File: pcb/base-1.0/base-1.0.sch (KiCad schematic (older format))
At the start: 80 parts, among them J101 USB_B_Micro, J102 UART, J103 74984104400, J104 Jack-DC, J105 USB_GPIO, J106 Raspberry_Pi_2_3, Q101 BC817, Q102 BC817, Q103 DMP2305U-7, SW101 SW_Push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

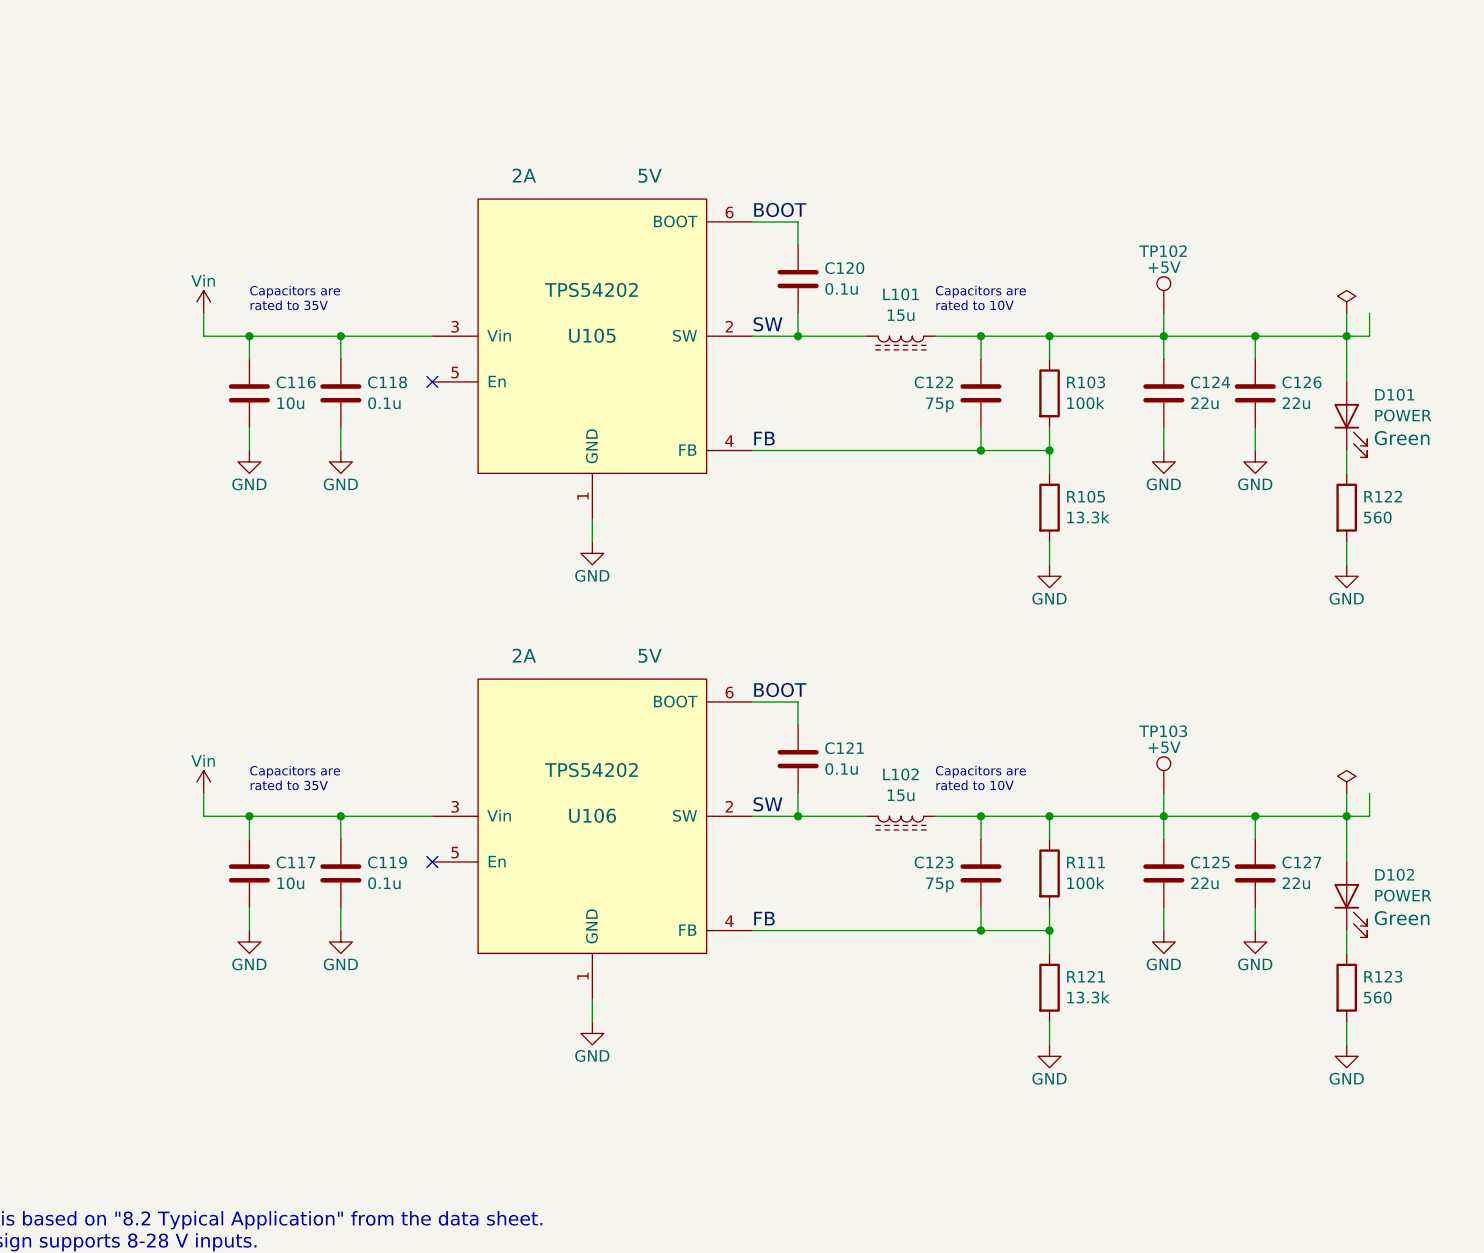
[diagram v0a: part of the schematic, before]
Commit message: o Adjusting text size from 60 to 50 mil for imported DC/DC schematic.
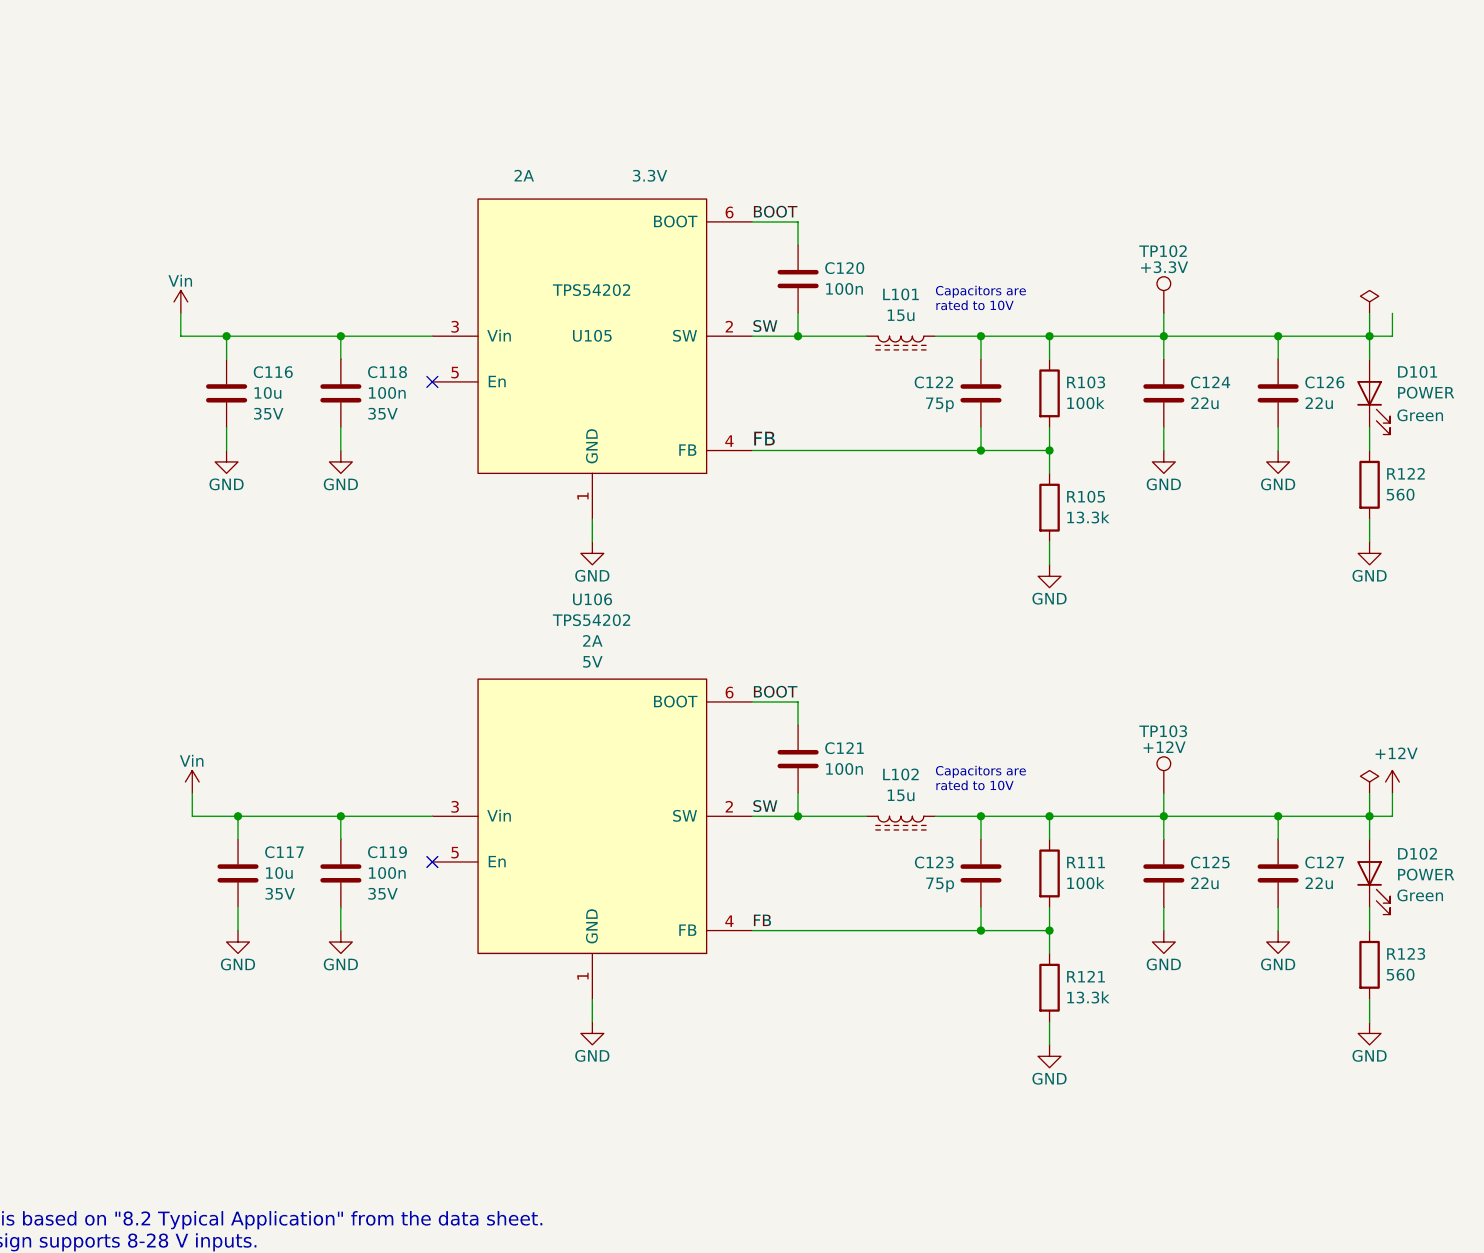
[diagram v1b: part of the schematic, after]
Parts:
- C118, C119, C120, C121: value 0.1u -> 100n
- TP102: value +5V -> +3.3V
- TP103: value +5V -> +12V
- U105: Vout 5V -> 3.3V
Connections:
- net +12V: now reaches C123.1, C125.1, C127.1, D102.2 (A), L102.1, R111.1, TP103.1
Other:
- note removed: "Capacitors are\nrated to 35V"
- moved on the sheet: C116, C117, C126, C127, D101, D102, R122, R123

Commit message: o More values.
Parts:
- C104: value C -> 1n; voltage (none) -> 2kV
- C113: value C -> ~
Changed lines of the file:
@@
 U 1 1 5DBE189D
 P 1900 10750
-F 0 "C104" H 2015 10796 50  0000 L CNN
-F 1 "C" H 2015 10705 50  0000 L CNN
+F 0 "C104" H 2015 10841 50  0000 L CNN
+F 1 "1n" H 2015 10750 50  0000 L CNN
 F 2 "IPC-7351-CAPC:CAPC_1005x015" H 1938 10600 50  0001 C CNN
 F 3 "~" H 1900 10750 50  0001 C CNN
+F 4 "2kV" H 2015 10659 50  0000 L CNN "voltage"
 	1    1900 10750
 	1    0    0    -1
@@
 U 1 1 5CEB2CA9
 P 700 2650
-F 0 "C113" H 815 2741 50  0000 L CNN
-F 1 "C" H 815 2650 50  0000 L CNN
+F 0 "C113" H 815 2696 50  0000 L CNN
+F 1 "~" H 815 2650 50  0000 L CNN
 F 2 "IPC-7351-CAPC:CAPC_1005x015" H 738 2500 50  0001 C CNN
 F 3 "~" H 700 2650 50  0001 C CNN
-F 4 "DNP" H 815 2559 50  0000 L CNN "populate"
+F 4 "DNP" H 815 2605 50  0000 L CNN "populate"
 	1    700  2650
 	1    0    0    -1

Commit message: o More values.
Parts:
- R106, R107: value R -> 120 Ω
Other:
- moved on the sheet: D104, R107
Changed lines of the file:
@@
 Text Label 5600 2700 0    50   ~ 0
 TXT
-$Comp
-L Device:LED D104
-U 1 1 5CC3EC2A
-P 7300 1950
-F 0 "D104" H 7293 1788 50  0000 C CNN
-F 1 "TX" H 7293 1697 50  0000 C CNN
-F 2 "IPC-7351-LEDSC:LEDSC_3216x060" H 7300 1950 50  0001 C CNN
-F 3 "~" H 7300 1950 50  0001 C CNN
-	1    7300 1950
-	0    -1   -1   0
-$EndComp
-$Comp
-L Device:R R107
-U 1 1 5CD8FDB9
-P 7300 2350
-F 0 "R107" V 7415 2350 50  0000 C CNN
-F 1 "R" V 7506 2350 50  0000 C CNN
-F 2 "IPC-7351-RESC:RESC_1005x015" V 7230 2350 50  0001 C CNN
-F 3 "~" H 7300 2350 50  0001 C CNN
-	1    7300 2350
-	1    0    0    -1
-$EndComp
-Wire Wire Line
-	7300 2200 7300 2100
 Wire Wire Line
 	7100 2200 7100 2100
-$Comp
-L Device:R R106
-U 1 1 5CD8FFCC
-P 7100 2350
-F 0 "R106" V 7307 2350 50  0000 C CNN
-F 1 "R" V 7216 2350 50  0000 C CNN
-F 2 "IPC-7351-RESC:RESC_1005x015" V 7030 2350 50  0001 C CNN
-F 3 "~" H 7100 2350 50  0001 C CNN
-	1    7100 2350
-	-1   0    0    1
-$EndComp
-$Comp
-L Device:LED D103
-U 1 1 5CC3BC53
-P 7100 1950
-F 0 "D103" H 7093 2166 50  0000 C CNN
-F 1 "RX" H 7093 2075 50  0000 C CNN
-F 2 "IPC-7351-LEDSC:LEDSC_3216x060" H 7100 1950 50  0001 C CNN
-F 3 "~" H 7100 1950 50  0001 C CNN
-	1    7100 1950
-	0    -1   -1   0
-$EndComp
 Wire Wire Line
 	4300 900  4900 900
@@
 Wire Wire Line
 	7100 1600 7100 1700
-Wire Wire Line
-	7300 1800 7300 1700
-Wire Wire Line
-	7300 1700 7100 1700
 Connection ~ 7100 1700
 Wire Wire Line
@@
 	7100 2500 7100 2600
 Wire Wire Line
-	7300 2500 7300 2700
-Wire Wire Line
 	5600 2600 7100 2600
-Wire Wire Line
-	5600 2700 7300 2700
 $Comp
 L Device:Q_NPN_BEC Q102
@@
 	1    0    0    -1
 $EndComp
+$Comp
+L Device:LED D103
+U 1 1 5CC3BC53
+P 7100 1950
+F 0 "D103" V 7139 1832 50  0000 R CNN
+F 1 "RX" V 7048 1832 50  0000 R CNN
+F 2 "IPC-7351-LEDSC:LEDSC_3216x060" H 7100 1950 50  0001 C CNN
+F 3 "~" H 7100 1950 50  0001 C CNN
+	1    7100 1950
+	0    -1   -1   0
+$EndComp
+Wire Wire Line
+	5600 2700 7500 2700
+Wire Wire Line
+	7500 2500 7500 2700
+Wire Wire Line
+	7500 1700 7100 1700
+Wire Wire Line
+	7500 1800 7500 1700
+Wire Wire Line
+	7500 2200 7500 2100
+$Comp
+L Device:LED D104
+U 1 1 5CC3EC2A
+P 7500 1950
+F 0 "D104" V 7539 1832 50  0000 R CNN
+F 1 "TX" V 7448 1832 50  0000 R CNN
+F 2 "IPC-7351-LEDSC:LEDSC_3216x060" H 7500 1950 50  0001 C CNN
+F 3 "~" H 7500 1950 50  0001 C CNN
+	1    7500 1950
+	0    -1   -1   0
+$EndComp
+$Comp
+L Device:R R106
+U 1 1 5CD8FFCC
+P 7100 2350
+F 0 "R106" H 7030 2304 50  0000 R CNN
+F 1 "120 Ω" H 7030 2395 50  0000 R CNN
+F 2 "IPC-7351-RESC:RESC_1005x015" V 7030 2350 50  0001 C CNN
+F 3 "~" H 7100 2350 50  0001 C CNN
+	1    7100 2350
+	-1   0    0    1
+$EndComp
+$Comp
+L Device:R R107
+U 1 1 5CD8FDB9
+P 7500 2350
+F 0 "R107" H 7570 2396 50  0000 L CNN
+F 1 "120 Ω" H 7570 2305 50  0000 L CNN
+F 2 "IPC-7351-RESC:RESC_1005x015" V 7430 2350 50  0001 C CNN
+F 3 "~" H 7500 2350 50  0001 C CNN
+	1    7500 2350
+	1    0    0    -1
+$EndComp

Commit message: o Selecting parts.
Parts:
- C101: value 100n -> 100nF; mpn (none) -> CL05B104KO5NNNC
- C102: value 10u -> 10uF; footprint IPC-7351-CAPC:CAPC_1005x015 -> IPC-7351-CAPC:CAPC_2012x040; mpn (none) -> CL21B106KOQNNNE
- C104: value 1n -> 1nF; Voltage (none) -> 2kV; mpn (none) -> C1812C102KGRACAUTO; voltage 2kV -> (none)
- C105: mpn (none) -> CL05B471JB5NNNC
- C106, C109: mpn (none) -> CL05A105MQ5NNNC
- C107, C110, C111, C112, C115: mpn (none) -> CL05B104KO5NNNC
- C114: value 1u -> 1uF; mpn (none) -> CL05A105MQ5NNNC
- C116, C117: value 10u -> 10uF; Voltage (none) -> 35V; req_voltage 35V -> (none)
- C118, C119: value 100n -> 100nF; Voltage (none) -> 35V; mpn GMK212BJ104KGHT -> CL21B104MBCNNNC; req_voltage 35V -> (none)
- C120: value 100n -> 100nF; footprint IPC-7351-CAPC:CAPC_2012x040 -> IPC-7351-CAPC:CAPC_1005x015; Voltage (none) -> 35V; req_voltage (none) -> 10V; voltage 10V -> (none)
- C121: value 100n -> 100nF; footprint IPC-7351-CAPC:CAPC_2012x040 -> IPC-7351-CAPC:CAPC_1005x015; Voltage (none) -> 35V; req_voltage (none) -> 25V; voltage 10V -> (none)
- C122: value 75p -> 56pF; Voltage (none) -> 10V; mpn GRM1555C1H750JA01D -> CL05C560JB5NNNC; voltage 10V -> (none)
- C123: value 75p -> 100pF; Voltage (none) -> 25V; mpn GRM1555C1H750JA01D -> CL05C101JB5NNNC; voltage 10V -> (none)
- C124, C126: value 22u -> 22uF; Voltage (none) -> 10V; voltage 10V -> (none)
- C125, C127: value 22u -> 22uF; Voltage (none) -> 25V; voltage 10V -> (none)
- D101: I (none) -> 5 mA; V (none) -> 3.3; ds_Vf 2.1 V -> (none); req_I 5 mA -> (none); req_Vf 2.0 V -> (none); req_Vin 5V -> (none)
- D102: I (none) -> 5 mA; Vf (none) -> ?; Vin (none) -> ?; ds_Vf 2.1 V -> (none); req_I 5 mA -> (none); req_Vf 2.0 V -> (none); req_Vin 5V -> (none)
- L101: value 15u -> 10uH; footprint Inductors_SMD:L_Taiyo-Yuden_NR-80xx -> (none); mpn NRS8040T150MJGJ -> (none)
- L102: value 15u -> 22uH; footprint Inductors_SMD:L_Taiyo-Yuden_NR-80xx -> (none); mpn NRS8040T150MJGJ -> (none)
- R105: value 13.3k -> 22.1k
- R108: Tolerance (none) -> 1%; tollerance 1% -> (none)
- R121: value 13.3k -> 5.23k
- R122, R123: value 560 -> ~
- TP102, TP103: footprint Connectors_TestPoints:Test_Point_Pad_d1.0mm -> TestPoint:TestPoint_Pad_D1.0mm
- U105: footprint TO_SOT_Packages_SMD:SOT-23-6_Handsoldering -> Package_TO_SOT_SMD:SOT-23-6
- U106: footprint TO_SOT_Packages_SMD:SOT-23-6_Handsoldering -> Package_TO_SOT_SMD:SOT-23-6; Vout 5V -> 12V
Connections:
- net +3V3: now also C122.1, C124.1, C126.1, D101.2 (A), L101.1, R103.1, TP102.1
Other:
- note removed: "Design is based on "8.2 Typical Application" from the data sheet.\nThe design supports 8-28 V inputs.\nEN has internal pull up."
- moved on the sheet: C102

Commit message: o Selecting parts.
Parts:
- C103, C108: mpn (none) -> CL05A475MQ5NRNC
- Q103: mpn (none) -> DMP2305U-7
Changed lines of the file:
@@
 F 2 "IPC-7351-CAPC:CAPC_1005x015" H 5538 7700 50  0001 C CNN
 F 3 "~" H 5500 7850 50  0001 C CNN
+F 4 "CL05A475MQ5NRNC" H 5500 7850 50  0001 C CNN "mpn"
 	1    5500 7850
 	-1   0    0    -1
@@
 F 1 "DMP2305U-7" V 8152 6900 50  0000 C CNN
 F 2 "Package_TO_SOT_SMD:SOT-23" H 8100 7000 50  0001 C CNN
-F 3 "~" H 7900 6900 50  0001 C CNN
+F 3 "https://www.diodes.com/assets/Datasheets/ds31737.pdf" H 7900 6900 50  0001 C CNN
+F 4 "DMP2305U-7" H 7900 6900 50  0001 C CNN "mpn"
 	1    7900 6900
 	0    -1   -1   0
@@
 F 2 "IPC-7351-CAPC:CAPC_1005x015" H 3438 1300 50  0001 C CNN
 F 3 "~" H 3400 1450 50  0001 C CNN
+F 4 "CL05A475MQ5NRNC" H 3400 1450 50  0001 C CNN "mpn"
 	1    3400 1450
 	1    0    0    1

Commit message: o Trying to fix bad symbols for the TPS54202 designs.
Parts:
- U105, U106: mpn TPS54202DDCT -> (none); ta Figure 16. 5-V, 2-A Reference Design -> (none)
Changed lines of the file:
@@
 F 1 "POWER" V 15601 6732 50  0000 R CNN
 F 2 "IPC-7351-LEDSC:LEDSC_3216x060" H 15600 6850 50  0001 C CNN
-F 3 "" H 15600 6850 50  0001 C CNN
+F 3 "~" H 15600 6850 50  0001 C CNN
 F 4 "Green" V 15502 6732 50  0000 R CNN "color"
 F 5 "CMD15-21VGD/TR8" H 15600 6850 50  0001 C CNN "mpn"
@@
 $EndComp
 $Comp
-L tps54202:TPS54202 U?
-U 1 1 5DDFE462
+L tps54202:TPS54202 U105
+U 1 1 5CEE0940
 P 12200 6600
-AR Path="/5CB5BC22/5DDFE462" Ref="U?"  Part="1"
-AR Path="/5DDFE462" Ref="U105"  Part="1"
-AR Path="/5D709363/5DDFE462" Ref="U?"  Part="1"
-F 0 "U105" H 12200 7547 50  0000 C CNN
-F 1 "TPS54202" H 12200 7456 50  0000 C CNN
+F 0 "U105" H 12200 7400 50  0000 C CNN
+F 1 "TPS54202" H 12200 7300 50  0000 C CNN
 F 2 "Package_TO_SOT_SMD:SOT-23-6" H 12200 6600 50  0001 C CNN
 F 3 "http://www.ti.com/lit/ds/symlink/tps54202.pdf" H 12200 6600 50  0001 C CNN
-F 4 "Figure 16. 5-V, 2-A Reference Design" H 12200 6600 50  0001 C CNN "ta"
-F 5 "TPS54202DDCT" H 12200 6600 50  0001 C CNN "mpn"
-F 6 "2A" H 12200 7365 50  0000 C CNN "Iout"
-F 7 "3.3V" H 12200 7274 50  0000 C CNN "Vout"
+F 4 "2A" H 12500 7300 50  0000 L CNN "Iout"
+F 5 "3.3V" H 12500 7400 50  0000 L CNN "Vout"
 	1    12200 6600
 	1    0    0    -1
 $EndComp
 $Comp
-L tps54202:TPS54202 U?
-U 1 1 5DE4306A
+L tps54202:TPS54202 U106
+U 1 1 5CF0858B
 P 12200 8700
-AR Path="/5CB5BC22/5DE4306A" Ref="U?"  Part="1"
-AR Path="/5DE4306A" Ref="U106"  Part="1"
-AR Path="/5D709363/5DE4306A" Ref="U?"  Part="1"
-F 0 "U106" H 12200 9647 50  0000 C CNN
-F 1 "TPS54202" H 12200 9556 50  0000 C CNN
+F 0 "U106" H 12200 9500 50  0000 C CNN
+F 1 "TPS54202" H 12200 9400 50  0000 C CNN
 F 2 "Package_TO_SOT_SMD:SOT-23-6" H 12200 8700 50  0001 C CNN
 F 3 "http://www.ti.com/lit/ds/symlink/tps54202.pdf" H 12200 8700 50  0001 C CNN
-F 4 "Figure 16. 5-V, 2-A Reference Design" H 12200 8700 50  0001 C CNN "ta"
-F 5 "TPS54202DDCT" H 12200 8700 50  0001 C CNN "mpn"
-F 6 "2A" H 12200 9465 50  0000 C CNN "Iout"
-F 7 "12V" H 12200 9374 50  0000 C CNN "Vout"
+F 4 "2A" H 12500 9400 50  0000 L CNN "Iout"
+F 5 "12V" H 12500 9500 50  0000 L CNN "Vout"
 	1    12200 8700
 	1    0    0    -1
